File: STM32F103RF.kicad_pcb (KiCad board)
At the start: 2 copper layers, 59 parts, among them J1 USB_A, J4 Conn_Coaxial, U1 SPX3819M5-L-3-3, U2 STM32F103C6Tx, U3 NRF24L01, Y1 16MHz, Y2 16MHz

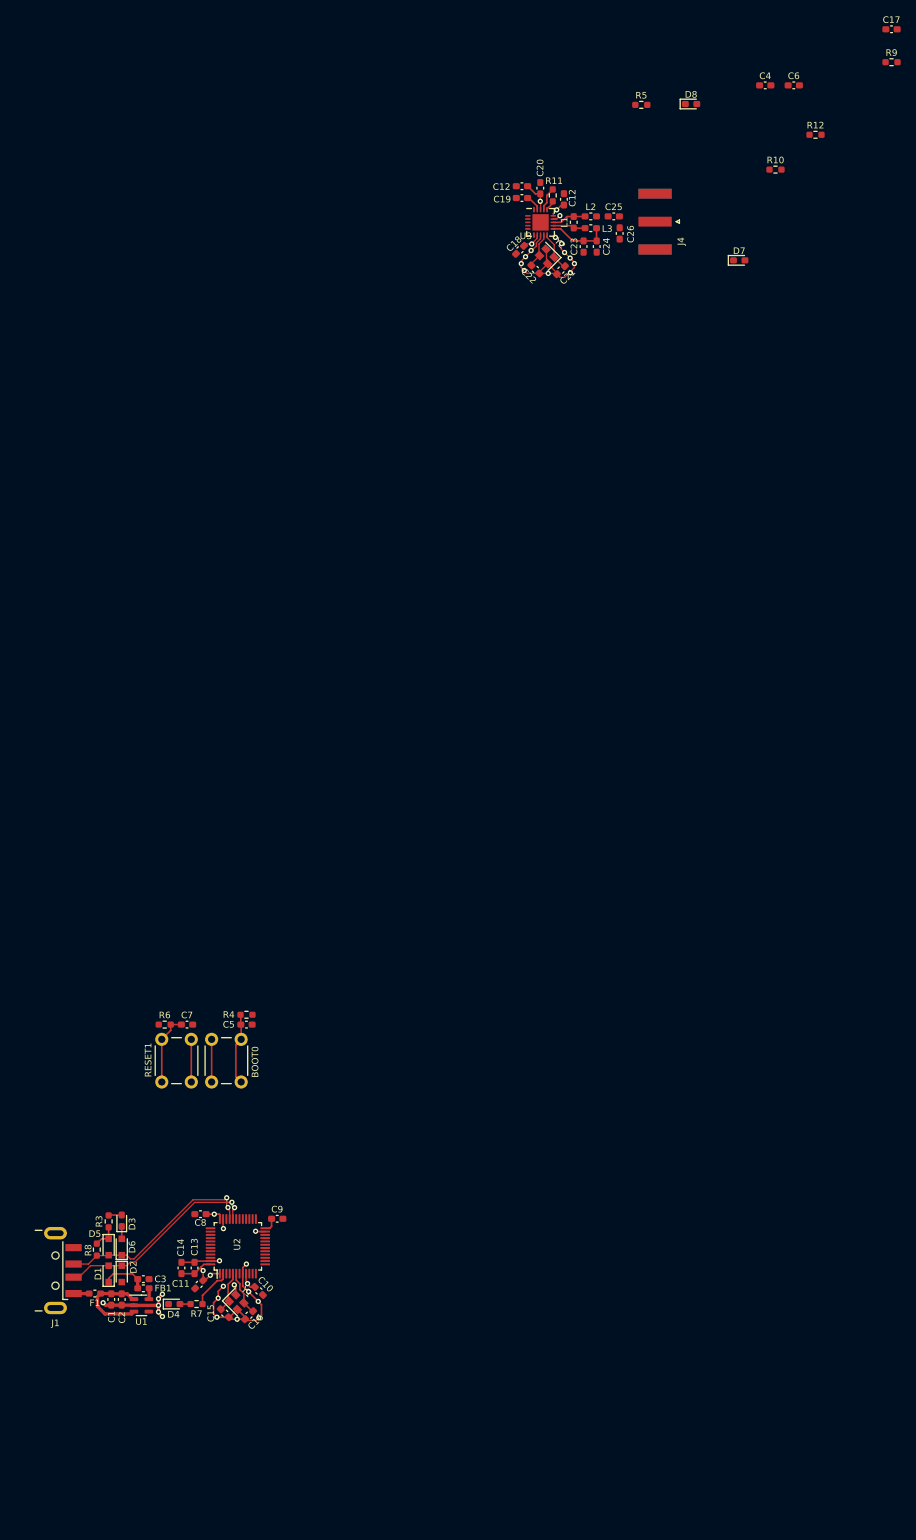
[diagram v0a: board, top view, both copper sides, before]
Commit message: placing usb components
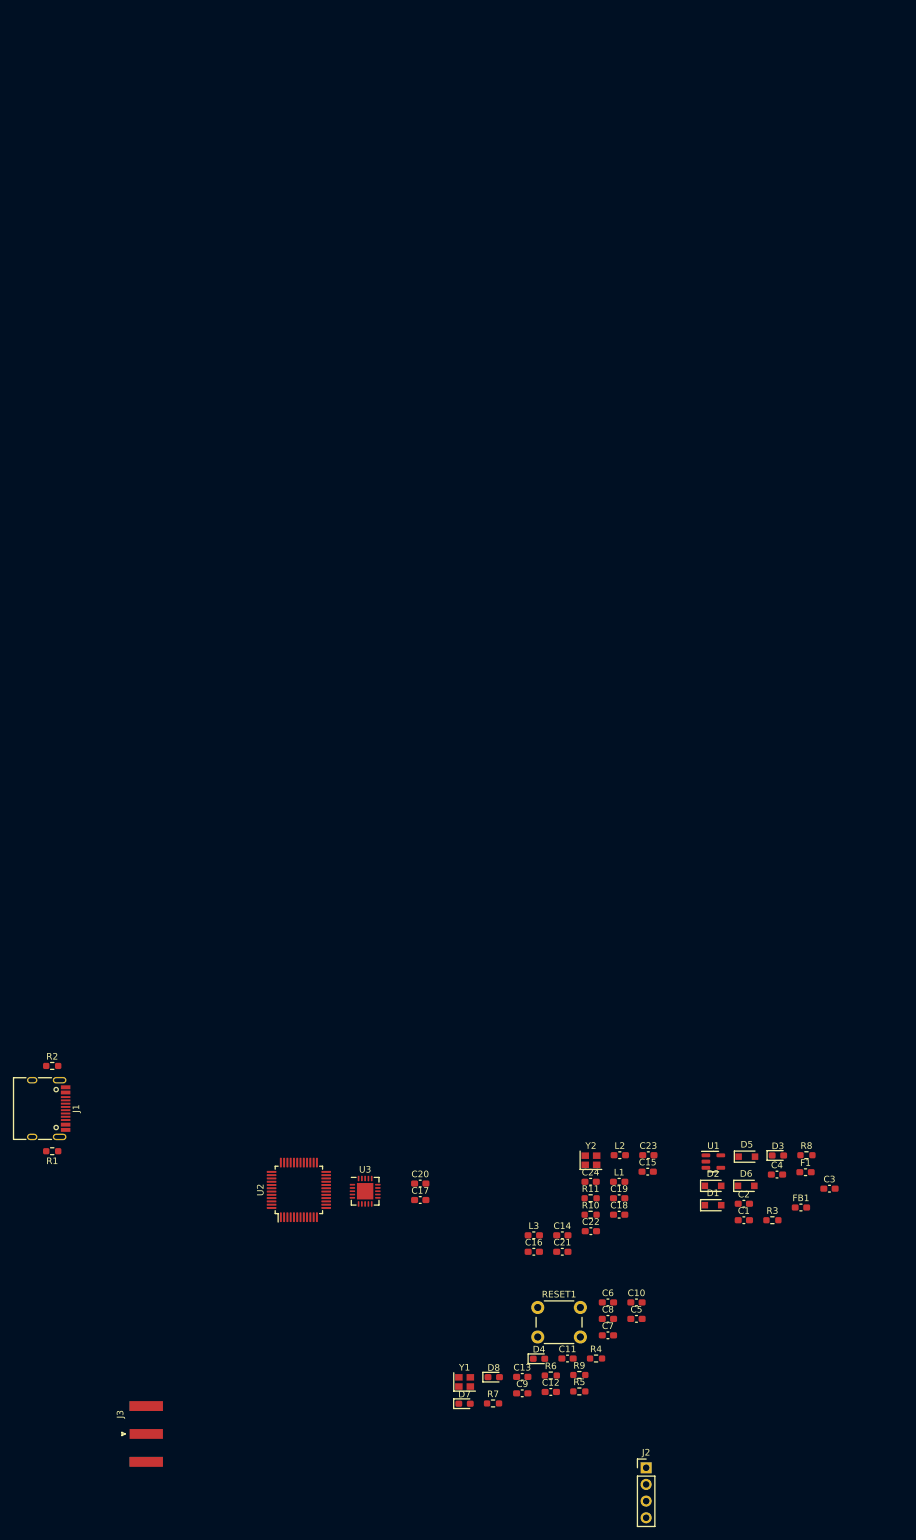
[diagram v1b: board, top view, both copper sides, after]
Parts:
- removed BOOT0: BOOT0, Button_Switch_THT:SW_PUSH_6mm
- removed the C12 at (103.6, -90.6)
- removed the C12 at (110.0, -88.6)
- removed C25: 1.5pF, Capacitor_SMD:C_0603_1608Metric_Pad1.08x0.95mm_HandSolder
- removed C26: 1pF, Capacitor_SMD:C_0603_1608Metric_Pad1.08x0.95mm_HandSolder
- removed J4: Conn_Coaxial, Connector_Coaxial:SMA_Amphenol_132289_EdgeMount
- removed R12: 1M, Resistor_SMD:R_0603_1608Metric_Pad0.98x0.95mm_HandSolder
- added C12: 10u, Capacitor_SMD:C_0603_1608Metric_Pad1.08x0.95mm_HandSolder, F.Cu at (108.0, 93.2)
- added J2: Conn_01x04, Connector_PinHeader_2.54mm:PinHeader_1x04_P2.54mm_Vertical, F.Cu at (122.5, 104.8)
- added J3: Conn_Coaxial, Connector_Coaxial:SMA_Amphenol_132289_EdgeMount, F.Cu at (46.3, 99.6)
- added R1: 5.1k, Resistor_SMD:R_0603_1608Metric_Pad0.98x0.95mm_HandSolder, F.Cu at (32.0, 56.5)
- added R2: 5.1k, Resistor_SMD:R_0603_1608Metric_Pad0.98x0.95mm_HandSolder, F.Cu at (32.0, 43.5)
- C13, C9: value 100n -> 10p
- C14: value 10u -> 100n
- C15, C16: value 10p -> 100n
- C17: value 10u -> 33nF
- C18: value 100n -> 10u
- C19: value 33nF -> 2.2nF
- C20: value 10u -> 4.7pF
- C21: value 10p -> 1.5pF
- C22: value 10p -> 1pF
- C23: value 2.2nF -> 10p
- C24: value 4.7pF -> 10p
- J1: value USB_A -> USB_C_Receptacle_USB2.0; footprint Connector_USB:USB_A_CNCTech_1001-011-01101_Horizontal -> Connector_USB:USB_C_Receptacle_HRO_TYPE-C-31-M-12
- R10: value 300 -> 22k
- R11: value 22k -> 1M
- R4, R6: value 10k -> 300
- R9: value 300 -> 10k
- moved R9 205.7 mm to (112.3, 90.6)
- moved D8 196.4 mm to (99.3, 90.9)
- moved R5 196.3 mm to (112.3, 93.1)
- moved C17 192.4 mm to (88.1, 63.9)
- moved C6 187.7 mm to (116.7, 79.5)
- moved D7 179.2 mm to (94.9, 95.0)
- moved C4 166.0 mm to (142.5, 60.1)
- moved R10 161.8 mm to (114.1, 66.2)
- moved L3 153.8 mm to (105.4, 69.3), turned to 0 degrees
- moved C19 153.2 mm to (118.4, 63.7)
- moved R11 153.0 mm to (114.1, 63.7), turned to 0 degrees
- moved C20 152.8 mm to (88.1, 61.4), turned to 0 degrees
- moved U3 150.1 mm to (79.7, 62.6)
- moved C21 149.6 mm to (109.8, 71.8), turned to 0 degrees
- moved C18 147.9 mm to (118.4, 66.2), turned to 0 degrees
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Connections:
- C10 pad 1: 3.3V -> NRST
- C13 pad 1: 3.3V -> PD1
- C15 pad 1: PD0 -> 3.3V
- C16 pad 1: PD1 -> 3.3V
- C17 pad 1: 3.3V -> GND
- C17 pad 2: GND -> Net-(C17-Pad2)
- C19 pad 2: Net-(C19-Pad2) -> VDD_PA
- C20 pad 1: 3.3V -> GND
- C20 pad 2: GND -> VDD_PA
- C21 pad 1: XC1 -> Net-(C21-Pad1)
- C21 pad 2: GND -> Net-(C21-Pad2)
- C22 pad 1: XC2 -> GND
- C22 pad 2: GND -> Net-(C21-Pad2)
- C23 pad 1: GND -> XC1
- C23 pad 2: VDD_PA -> GND
- C24 pad 1: GND -> XC2
- C24 pad 2: VDD_PA -> GND
- C5 pad 1: BOOT0 -> 3.3V
- C7 pad 1: NRST -> 3.3V
- C9 pad 1: 3.3V -> PD0
- F1 pad 1: Net-(F1-Pad1) -> V_USB
- L2 pad 2: Net-(C25-Pad1) -> Net-(C21-Pad1)
- R10 pad 1: Tx -> Net-(R10-Pad1)
- R10 pad 2: Net-(D8-Pad2) -> GND
- R11 pad 1: Net-(R11-Pad1) -> XC1
- R11 pad 2: GND -> XC2
- R4 pad 1: BOOT0 -> Rx
- R4 pad 2: GND -> Net-(D4-Pad2)
- R6 pad 1: 3.3V -> Tx
- R6 pad 2: NRST -> Net-(D7-Pad2)
- R7 pad 2: Net-(D4-Pad2) -> Net-(D8-Pad2)
- R9 pad 1: Rx -> 3.3V
- R9 pad 2: Net-(D7-Pad2) -> NRST
- U2 pad 13: RF_CE -> PA3
- U2 pad 14: RF_CSN -> PA4
- U2 pad 18: PB0 -> RF_CSN
- U2 pad 19: PB1 -> RF_CE
- U2 pad 37: PA14 -> SWCLK
- U2 pad 38: PA15 -> SWDIO
- U3 pad 16: Net-(R11-Pad1) -> Net-(R10-Pad1)
- U3 pad 19: Net-(C19-Pad2) -> Net-(C17-Pad2)
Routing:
- net GND: track 90.7 -> 0.00 mm, vias 30 -> 0
- net 3.3V: track 45.9 -> 0.00 mm, vias 7 -> 0
- net USB_D-: track 31.7 -> 0.00 mm, vias 2 -> 0
- net USB_D+: track 31.4 -> 0.00 mm, vias 2 -> 0
- net 5V: track 13.8 -> 0.00 mm
- net BOOT0: track 11.0 -> 0.00 mm
- net NRST: track 10.9 -> 0.00 mm
- net VDD_PA: track 9.33 -> 0.00 mm
- net PD1: track 6.86 -> 0.00 mm
- net PD0: track 6.39 -> 0.00 mm
- net PC13_LED: track 6.30 -> 0.00 mm
- net XC1: track 6.03 -> 0.00 mm
- net XC2: track 5.48 -> 0.00 mm
- net ANT2: track 5.22 -> 0.00 mm
- net ANT1: track 5.01 -> 0.00 mm
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
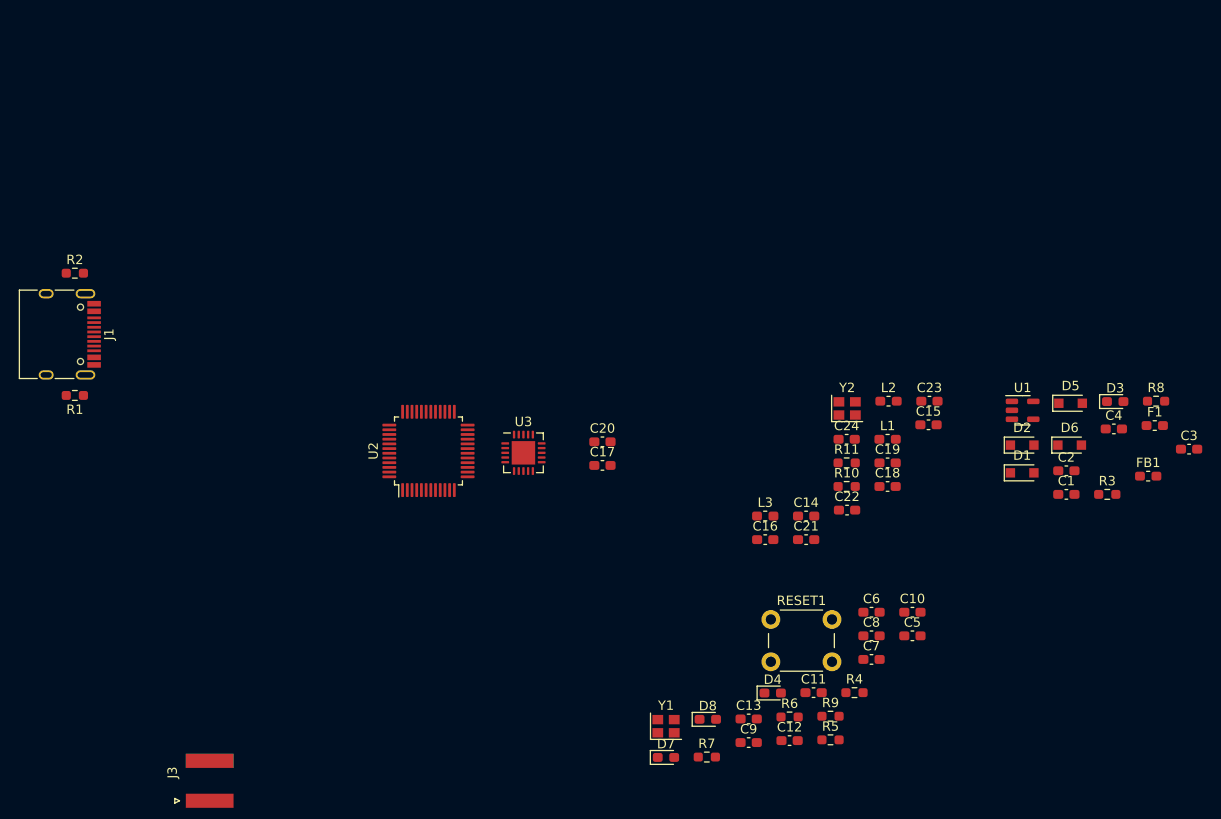
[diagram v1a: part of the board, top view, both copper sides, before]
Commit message: 4-layer stackup & some rough component placement
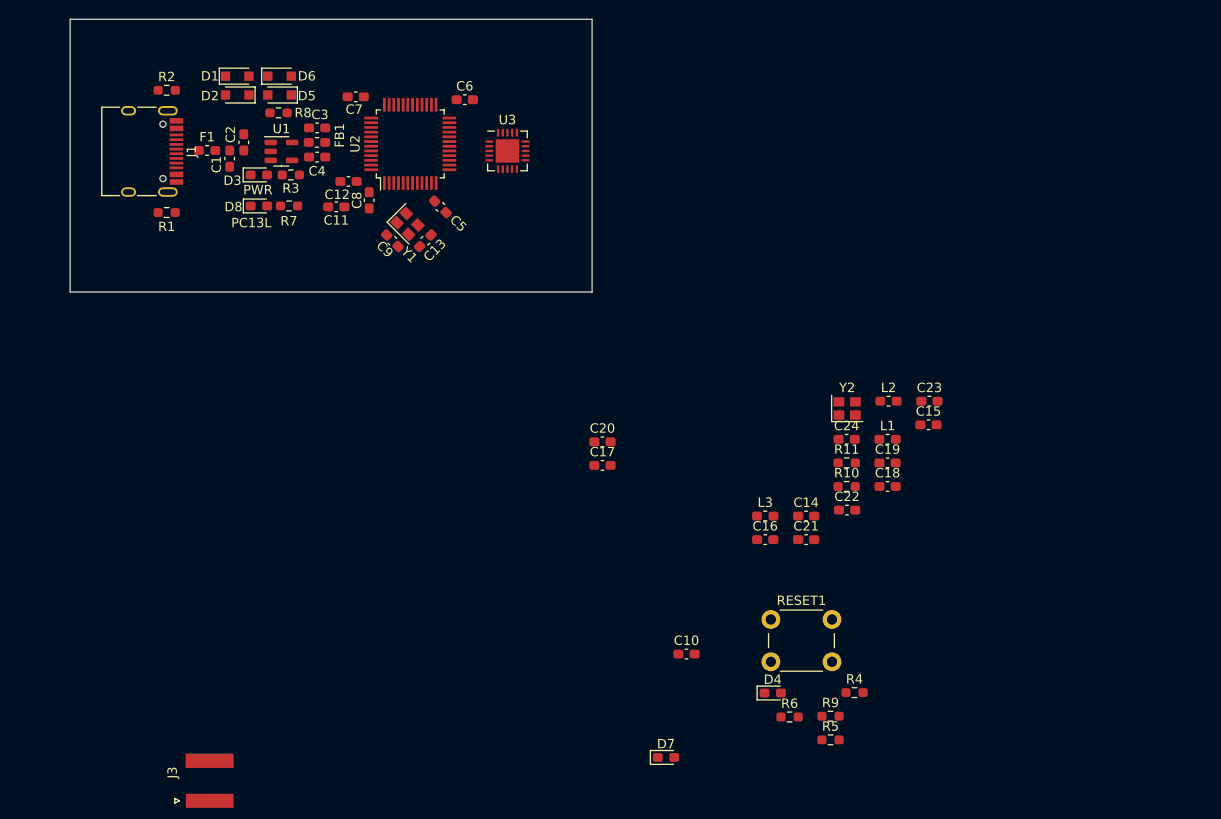
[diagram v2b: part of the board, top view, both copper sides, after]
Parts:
- moved F1 104.9 mm to (46.1, 30.4)
- moved C3 98.8 mm to (57.8, 28.1), turned to 180 degrees
- moved R8 98.2 mm to (53.7, 26.4), turned to 180 degrees
- moved C1 95.9 mm to (48.5, 31.3), turned to -90 degrees
- moved FB1 95.2 mm to (57.7, 29.6)
- moved D3 94.2 mm to (51.6, 33.0)
- moved C2 94.2 mm to (50.0, 29.6), turned to 90 degrees
- moved D1 93.5 mm to (49.3, 22.6)
- moved R3 93.2 mm to (55.0, 33.0), turned to 180 degrees
- moved D6 92.7 mm to (53.8, 22.6)
- moved D2 91.4 mm to (49.3, 24.6), turned to 180 degrees
- moved D5 90.3 mm to (53.8, 24.6), turned to 180 degrees
- moved C4 89.5 mm to (57.8, 31.1), turned to 180 degrees
- moved U1 83.5 mm to (54.0, 30.6)
- moved C7 81.2 mm to (61.9, 24.8), turned to 180 degrees
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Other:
- board outline added: 55.5 x 29 mm
- copper layers 2 -> 4
- board text added: "PC13L"
- board text added: "PWR"

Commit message: sum layouting
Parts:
- removed RESET1: RST, Button_Switch_THT:SW_PUSH_6mm
- moved J2 98.2 mm to (69.7, 22.0), turned to 90 degrees
- moved J3 87.1 mm to (99.5, 30.6)
- moved R4 84.3 mm to (48.9, 35.7), turned to -90 degrees
- moved R6 82.0 mm to (47.2, 35.7), turned to -90 degrees
- moved D4 75.4 mm to (48.9, 39.2), turned to 90 degrees
- moved D7 73.4 mm to (47.2, 39.2), turned to 90 degrees
- moved R9 73.2 mm to (59.8, 39.6), turned to 180 degrees
- moved R5 68.6 mm to (73.6, 36.5), turned to -45 degrees
- moved C10 59.2 mm to (59.8, 38.0)
- moved C18 56.1 mm to (78.6, 26.7)
- moved C15 54.3 mm to (74.9, 33.9), turned to 180 degrees
- moved C14 54.1 mm to (78.6, 25.1)
- moved R10 51.1 mm to (82.4, 26.1)
- moved C16 49.0 mm to (82.4, 28.6)
- moved C23 45.4 mm to (80.7, 40.2), turned to -135 degrees
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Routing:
- net GND: track 0.00 -> 196.1 mm, vias 0 -> 62
- net USB_D+: track 0.00 -> 54.8 mm, vias 0 -> 4
- net 3.3V: track 0.00 -> 53.5 mm, vias 0 -> 13
- net USB_D-: track 0.00 -> 50.1 mm, vias 0 -> 2
- net NRST: track 0.00 -> 18.4 mm, vias 0 -> 2
- net SWDIO: track 0.00 -> 13.8 mm, vias 0 -> 1
- net VDD_PA: track 0.00 -> 12.0 mm
- net PC13_LED: track 0.00 -> 11.9 mm, vias 0 -> 2
- net SWCLK: track 0.00 -> 10.8 mm, vias 0 -> 1
- net 5V: track 0.00 -> 10.2 mm
- net Net-(R5-Pad1): track 0.00 -> 9.34 mm, vias 0 -> 2
- net ANT1: track 0.00 -> 8.55 mm
- net XC1: track 0.00 -> 8.24 mm
- net V_USB: track 0.00 -> 8.20 mm
- net XC2: track 0.00 -> 8.14 mm
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- added copper zone on B.Cu, net 3.3V
- added copper zone on In1.Cu, net GND
- added copper zone on In2.Cu, net GND
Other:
- board size 55.5 x 29 mm -> 75 x 24 mm
- board text added: "3V3 | SWCLK"
- board text added: "3V3|SWCLK"
- board text added: "SWDIO|GND"

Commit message: fixing repo hopefully
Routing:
- net GND: track 196.1 -> 192.4 mm
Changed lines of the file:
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@@
   (segment (start 44.7 33.8) (end 44.7 34.8) (width 0.508) (layer "F.Cu") (net 1))
   (segment (start 44.7 33.8) (end 45.7 33.8) (width 0.508) (layer "F.Cu") (net 1))
-  (segment (start 90.3 24.1) (end 94 24.1) (width 0.508) (layer "F.Cu") (net 1))
   (segment (start 98.1 33.3) (end 98.1 34.8) (width 0.508) (layer "F.Cu") (net 1))
   (segment (start 103 25.2) (end 101.9 24.1) (width 0.508) (layer "F.Cu") (net 1))

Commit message: fixing repo hopefully
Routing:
- net GND: track 192.4 -> 196.1 mm
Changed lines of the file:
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@@
   (segment (start 55.25 23.4) (end 58.186985 23.4) (width 0.25) (layer "F.Cu") (net 1))
   (segment (start 75.6 24.4) (end 74.95 25.05) (width 0.25) (layer "F.Cu") (net 1))
+  (segment (start 90.3 24.1) (end 94 24.1) (width 0.508) (layer "F.Cu") (net 1))
   (segment (start 70.4 27.5) (end 70.3 27.6) (width 0.25) (layer "F.Cu") (net 1))
   (segment (start 75.3 39.1) (end 76.6 37.8) (width 0.25) (layer "F.Cu") (net 1))

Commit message: minor changes
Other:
- board size 75 x 24 mm -> 68 x 24 mm
- board text removed: "3V3 | SWCLK"
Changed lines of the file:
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@@
     )
   )
-  (gr_line (start 111 30) (end 107.1 30) (layer "Edge.Cuts") (width 0.1))
   (gr_line (start 103.97868 39.97868) (end 103.97868 22.02132) (layer "Edge.Cuts") (width 0.1))
   (gr_line (start 100.97868 19.02132) (end 39 19) (layer "Edge.Cuts") (width 0.1))
@@
     (effects (font (size 1 1) (thickness 0.15)))
   )
-  (gr_text "3V3 | SWCLK" (at 95.3 33.8) (layer "F.SilkS")
-    (effects (font (size 1 1) (thickness 0.15)))
-  )

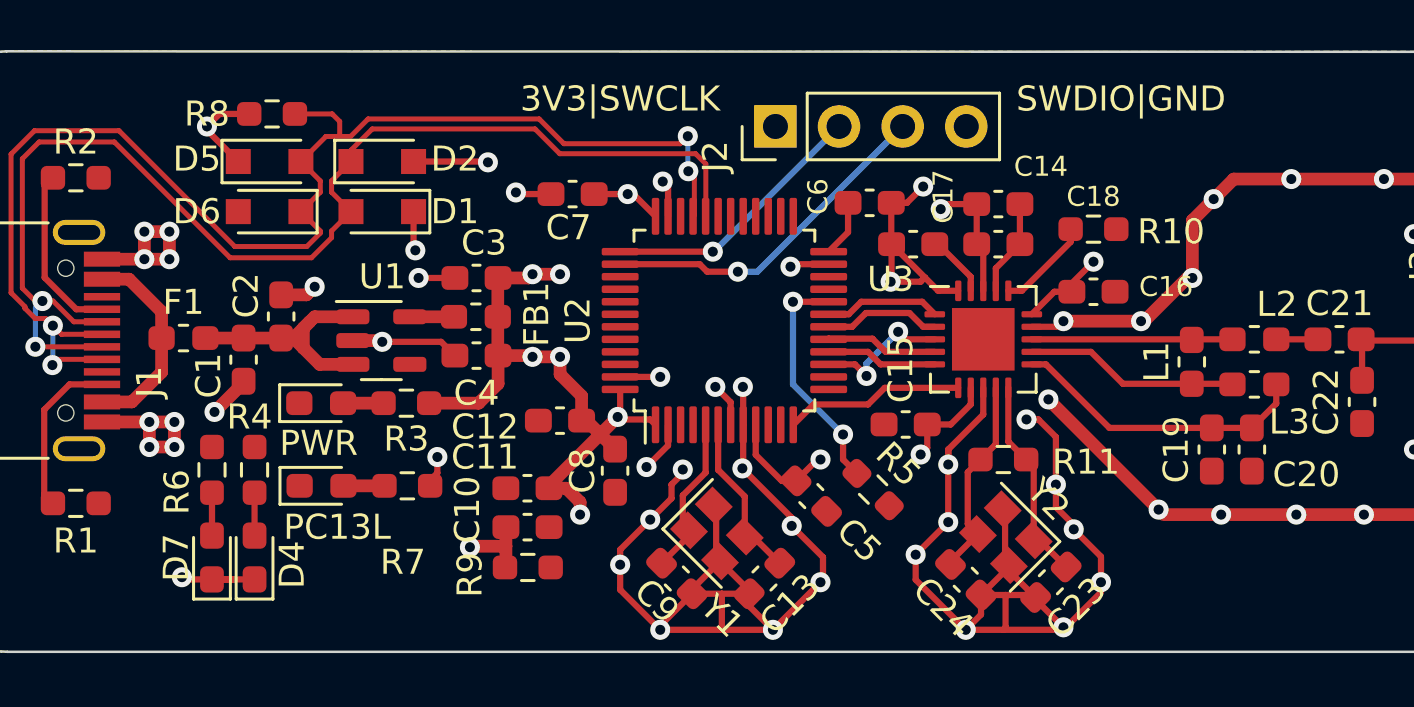
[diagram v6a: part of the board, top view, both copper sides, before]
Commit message: added usbc and crystal 3d models
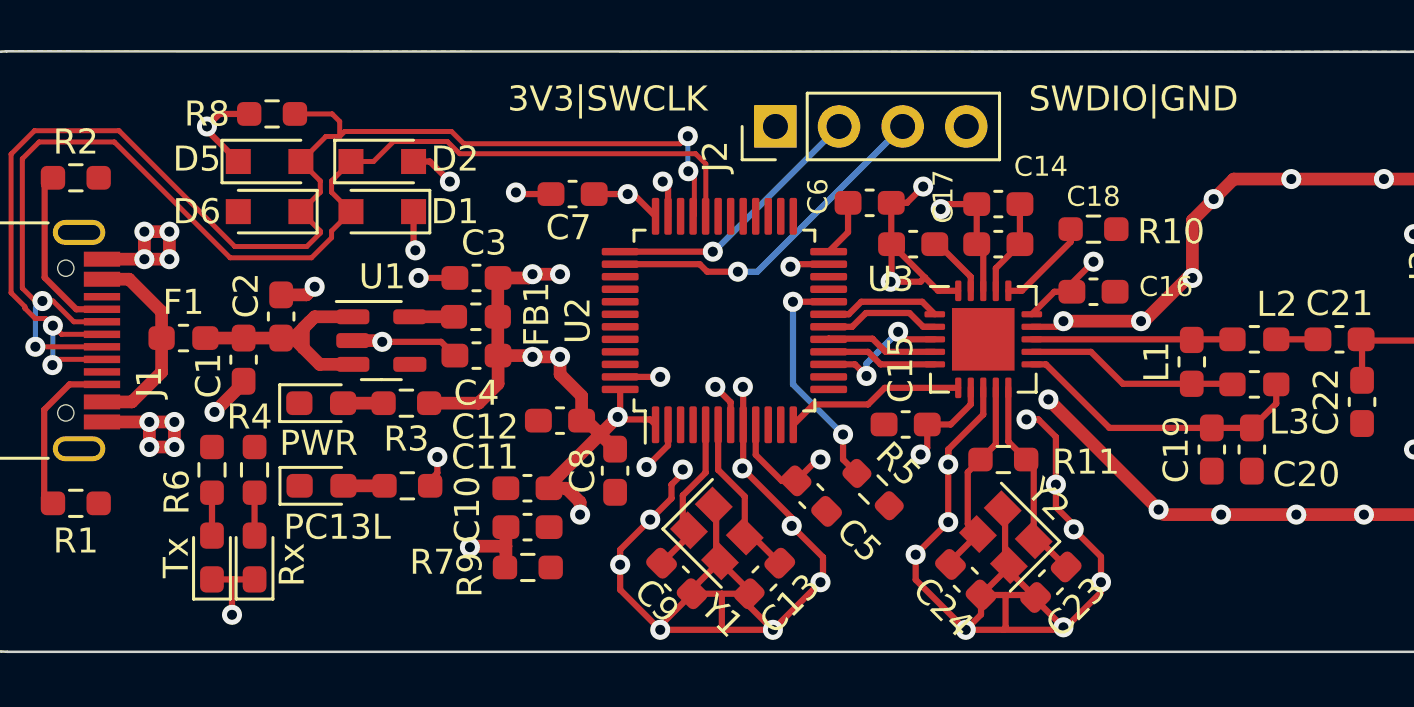
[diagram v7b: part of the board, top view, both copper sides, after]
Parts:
- renumbered D4 to Rx, D7 to Tx
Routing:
- net GND: track 196.1 -> 194.2 mm
- net USB_D-: track 50.1 -> 49.4 mm
